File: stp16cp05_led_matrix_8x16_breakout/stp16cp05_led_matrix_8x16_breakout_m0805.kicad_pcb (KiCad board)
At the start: 2 copper layers, 101 x 83 mm, 174 parts, among them J1 (Input) LED Matrix 2.54mm Fem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, J2 (Input) LED Matrix (SMD), Q1 DMP3125L-7, Q2 DMP3125L-7, Q3 DMP3125L-7, Q4 DMP3125L-7, Q5 DMP3125L-7, Q6 DMP3125L-7, Q7 DMP3125L-7, Q8 DMP3125L-7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

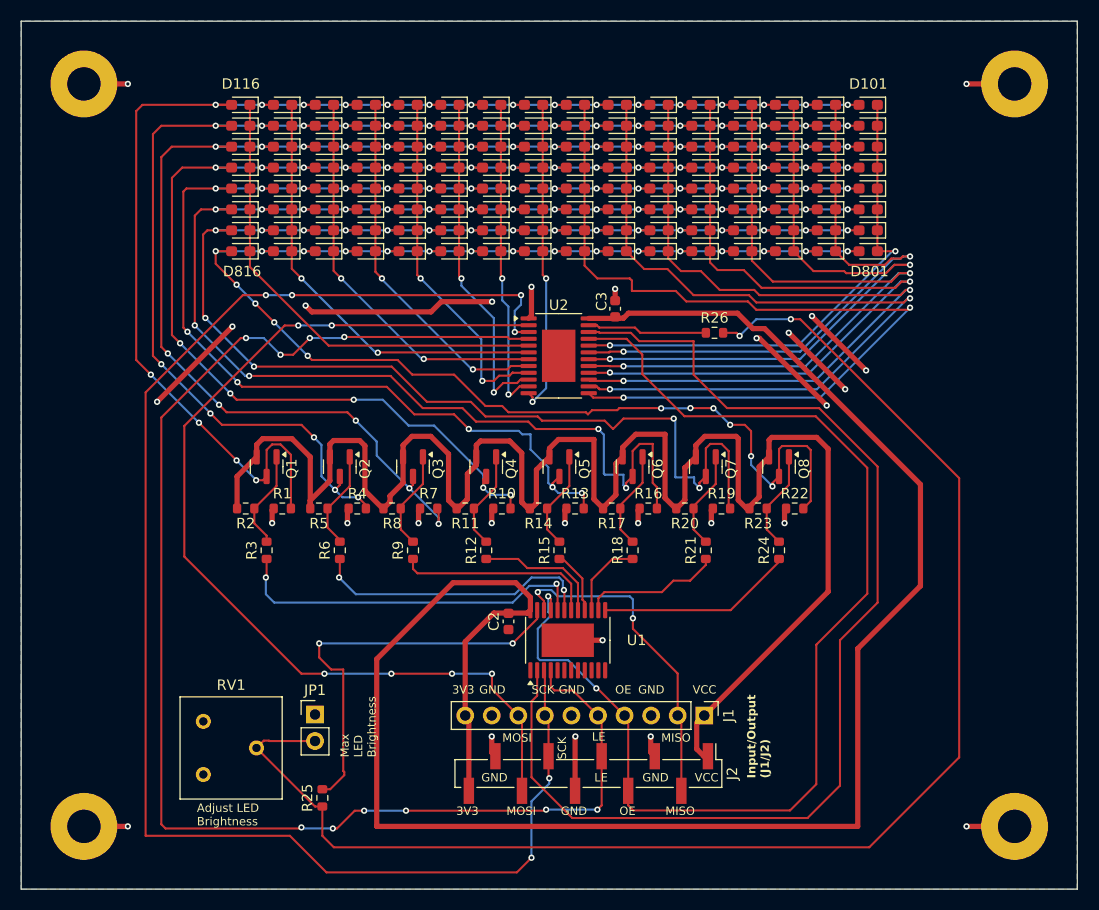
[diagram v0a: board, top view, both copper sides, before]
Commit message: Updated pcb
- D101 is now the most bottom left, going x01 to x116 from left to right
  and 1xx to 8xx going from bottom to top
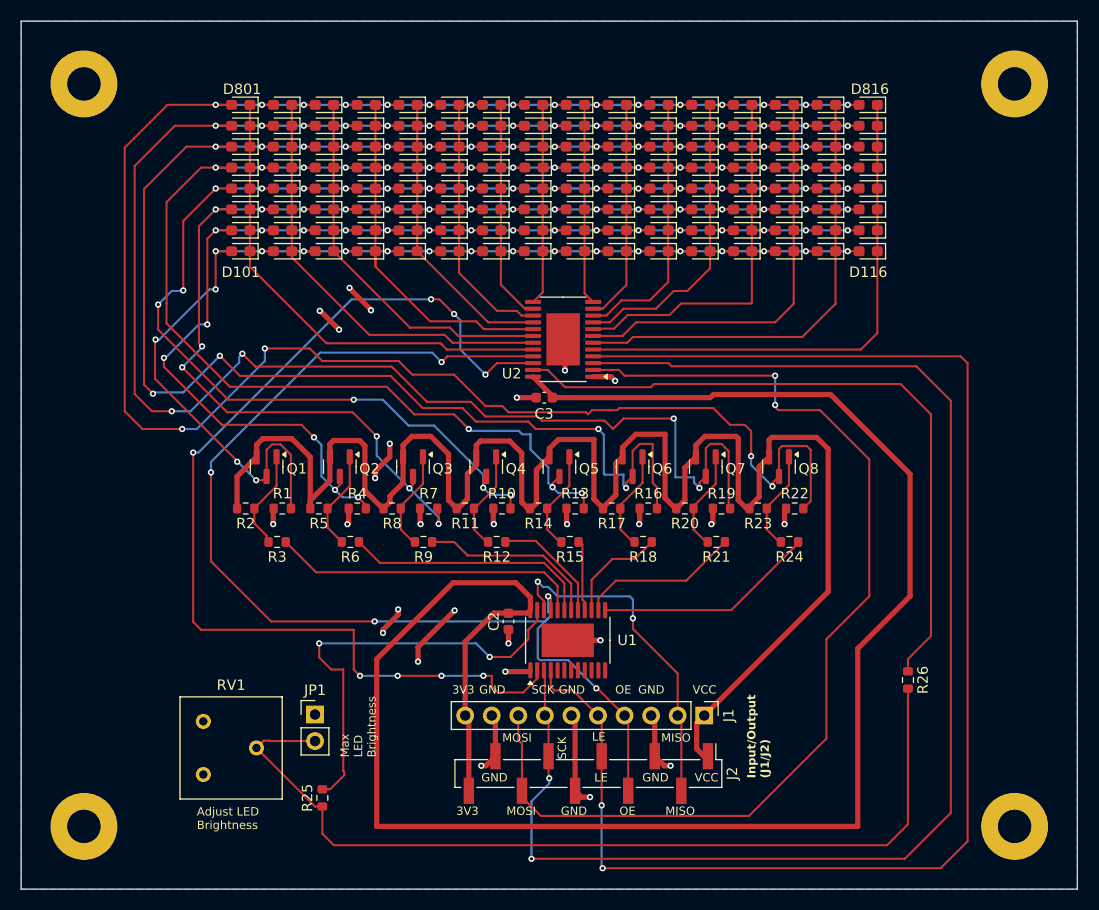
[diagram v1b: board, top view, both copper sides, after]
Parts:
- moved D101 61.6 mm to (160.0, 64.0)
- moved D116 61.6 mm to (220.0, 64.0)
- moved D801 61.6 mm to (160.0, 50.0)
- moved D816 61.6 mm to (220.0, 50.0)
- moved D201 60.8 mm to (160.0, 62.0)
- moved D216 60.8 mm to (220.0, 62.0)
- moved D701 60.8 mm to (160.0, 52.0)
- moved D716 60.8 mm to (220.0, 52.0)
- moved D301 60.3 mm to (160.0, 60.0)
- moved D316 60.3 mm to (220.0, 60.0)
- moved D601 60.3 mm to (160.0, 54.0)
- moved D616 60.3 mm to (220.0, 54.0)
- moved D401 60.0 mm to (160.0, 58.0)
- moved D416 60.0 mm to (220.0, 58.0)
- moved D501 60.0 mm to (160.0, 56.0)
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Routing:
- net /COL8: track 83.4 -> 19.2 mm, vias 2 -> 0
- net /COL7: track 77.4 -> 21.2 mm, vias 2 -> 0
- net /REXT2: track 11.5 -> 65.5 mm
- net Net-(JP1-B): track 138.6 -> 87.4 mm, vias 2 -> 0
- net /COL6: track 73.8 -> 24.8 mm, vias 2 -> 0
- net /ROW8: track 157.0 -> 201.4 mm, vias 26 -> 20
- net /COL5: track 69.7 -> 27.9 mm, vias 2 -> 0
- net GND: track 99.2 -> 65.6 mm, vias 28 -> 27
- net /COL4: track 65.6 -> 34.5 mm, vias 2 -> 0
- net /ROW7: track 158.4 -> 188.8 mm
- net /COL3: track 60.8 -> 36.6 mm, vias 2 -> 0
- net /ROW1: track 139.6 -> 119.0 mm
- net /ROW6: track 153.9 -> 173.9 mm
- net /COL2: track 56.5 -> 40.7 mm, vias 2 -> 0
- net /ROW2: track 135.7 -> 122.4 mm
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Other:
- board text removed: "D101 bottom left is v02"

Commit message: Update pcb (shcematic changes)
- Pull in changes to schematic
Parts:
- C2, C3: value 100n 16V -> 100n
- J1: value (Input) LED Matrix 2.54mm Female -> (Input/Output) LED Matrix 2.54mm Female
- J2: value (Input) LED Matrix (SMD) -> (Input/Output) LED Matrix (SMD)
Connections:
- net +3.3V renamed +3V3
